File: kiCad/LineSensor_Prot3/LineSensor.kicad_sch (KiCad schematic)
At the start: 145 parts, among them J1 Conn_01x04_Socket, J2 Conn_01x02_Socket, Q1 Q_Photo_NPN, Q10 Q_Photo_NPN, Q11 Q_Photo_NPN, Q12 Q_Photo_NPN, Q13 Q_Photo_NPN, Q14 Q_Photo_NPN, Q15 Q_Photo_NPN, Q16 Q_Photo_NPN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

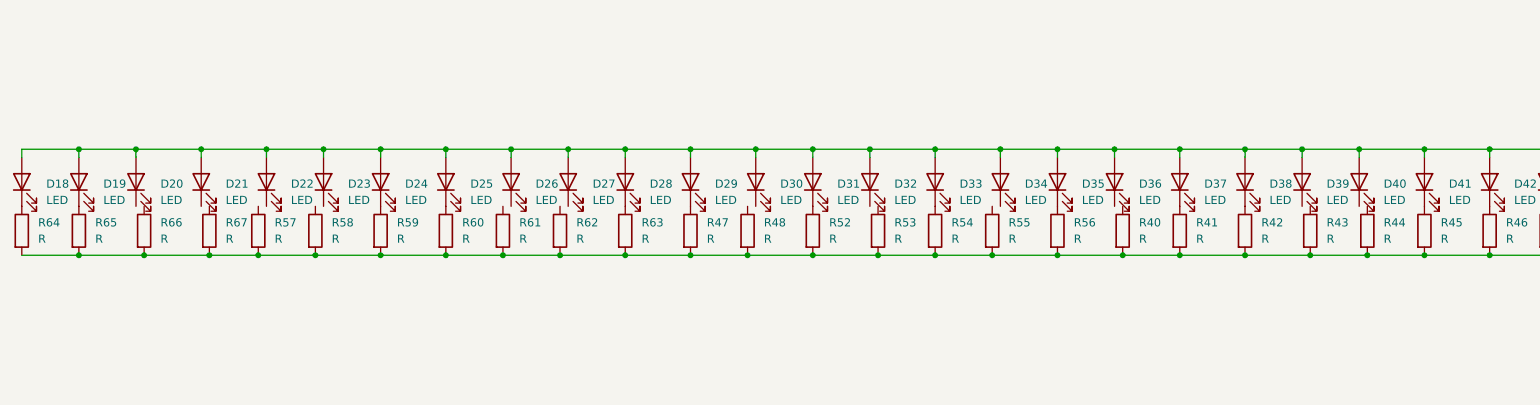
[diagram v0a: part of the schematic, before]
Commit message: 11/1夜_LED配置まで
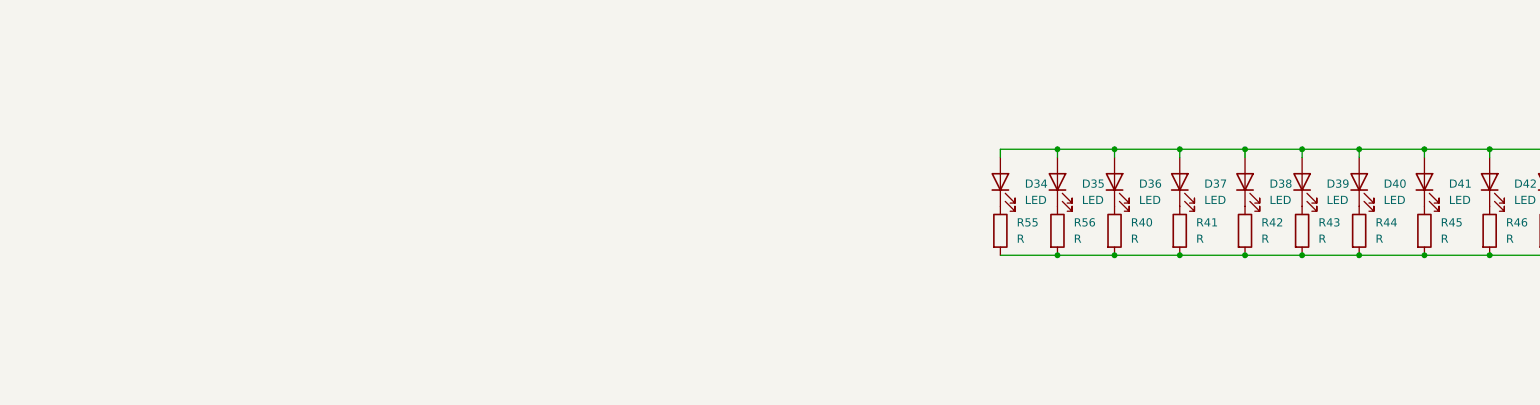
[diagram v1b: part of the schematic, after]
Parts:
- removed D18, D19, D20, D21, D22, D23, D24, D25, D26, D27, D28, D29, D30, D31, D32, D33: LED, LED_SMD:LED_0603_1608Metric, symbol Device:LED
- removed R47, R48, R52, R53, R54, R57, R58, R59, R60, R61, R62, R63, R64, R65, R66: R, Resistor_SMD:R_0603_1608Metric_Pad0.98x0.95mm_HandSolder, symbol Device:R
- removed R67: R, Capacitor_THT:CP_Radial_D5.0mm_P2.50mm, symbol Device:R
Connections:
- net at D39.1 (K): now also R43.1
- net at D36.1 (K): now also R40.1
- net at D34.1 (K): now also R55.1
- net at R44.1: now also D40.1 (K)
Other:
- moved on the sheet: R40, R43, R44, R55

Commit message: 円形配置 抵抗を平行に
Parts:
- removed U1: LM393, Package_SO:SOIC-8_3.9x4.9mm_P1.27mm, symbol Comparator:LM393
- added unit 2 of U9
- added unit 1 of U9
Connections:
- net GND: now also U2.4 (V-), U3.4 (V-), U4.4 (V-), U5.4 (V-); no longer U2.8 (V+), U3.8 (V+), U4.8 (V+), U5.8 (V+)
- net VCC: now also U2.8 (V+), U3.8 (V+), U4.8 (V+), U5.8 (V+); no longer U2.4 (V-), U3.4 (V-), U4.4 (V-), U5.4 (V-)
- net at A1.15 (D12), R30.2: now also U9.7
- net at Q14.2 (E), R18.1: now also U9.5 (+)
- net at RV4.2, U2.3 (+), U2.5 (+): now also U9.2 (-), U9.6 (-)
- net at Q13.2 (E), R17.1: now also U9.3 (+)
- net at A1.14 (D11), R29.2: now also U9.1
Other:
- moved on the sheet: U2C, U3C, U4C, U5C
